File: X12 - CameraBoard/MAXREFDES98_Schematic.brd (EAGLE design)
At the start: 87.8 x 25.4 mm, 26 parts, among them U1 MB110S-TP, U2 MB110S-TP, U3 MAX5969AETB+, U4 MAX17503ATP+

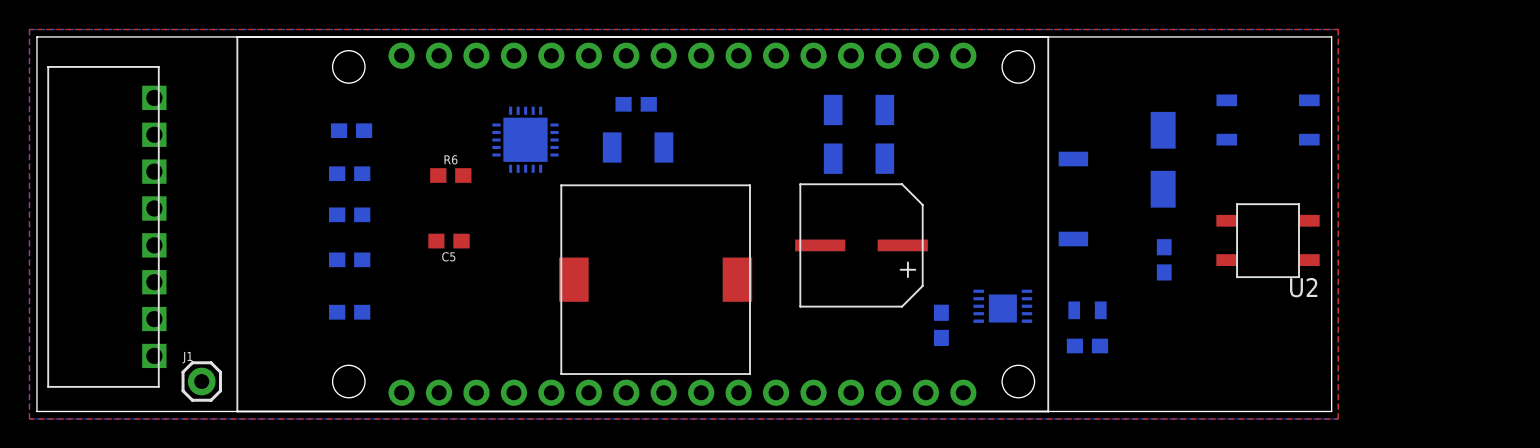
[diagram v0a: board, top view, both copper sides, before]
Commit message: Rerouting
Almost done, just need some clarification on the signals connected to the 8-pin connector before I try routing those. If the signals are as I assumed, the 8-pin connector might need to move to the other side of the board.
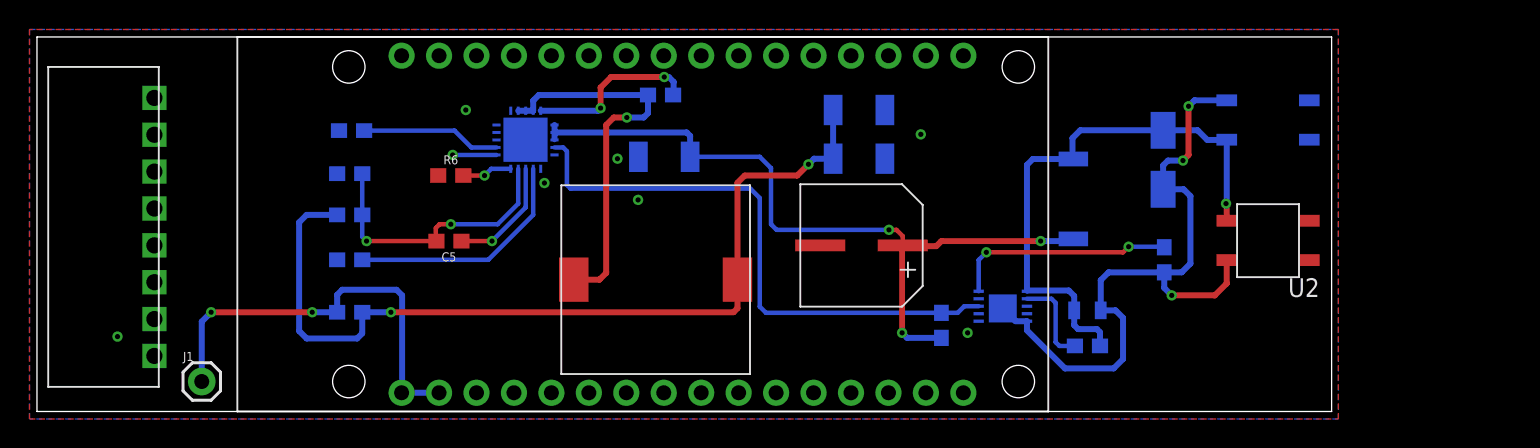
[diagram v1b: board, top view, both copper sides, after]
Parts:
- moved C7 1.89 mm to (42.5, 17.3)
- moved C9 1.77 mm to (42.3, 21.5)
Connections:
- net N$4 renamed CLS
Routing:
- net IND_2_OUT: track 0.00 -> 60.8 mm, vias 0 -> 2
- net VIN: track 0.00 -> 51.8 mm, vias 0 -> 3
- net VSS_EP: track 0.00 -> 47.3 mm, vias 0 -> 3
- net PG_EN/UVLO: track 0.00 -> 39.3 mm
- net VDD: track 0.00 -> 38.0 mm, vias 0 -> 1
- net 5V_OUT: track 0.00 -> 28.6 mm, vias 0 -> 2
- net LX: track 0.00 -> 26.6 mm, vias 0 -> 1
- net FB: track 0.00 -> 19.0 mm, vias 0 -> 2
- net SS: track 0.00 -> 16.0 mm
- net CLS: track 0.00 -> 15.1 mm, vias 0 -> 2
- net BST: track 0.00 -> 11.8 mm, vias 0 -> 2
- net VCC: track 0.00 -> 9.45 mm
- net CF: track 0.00 -> 7.92 mm, vias 0 -> 1
- net DET: track 0.00 -> 6.14 mm
- net RT: track 0.00 -> 3.40 mm, vias 0 -> 1
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
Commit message: Rerouting
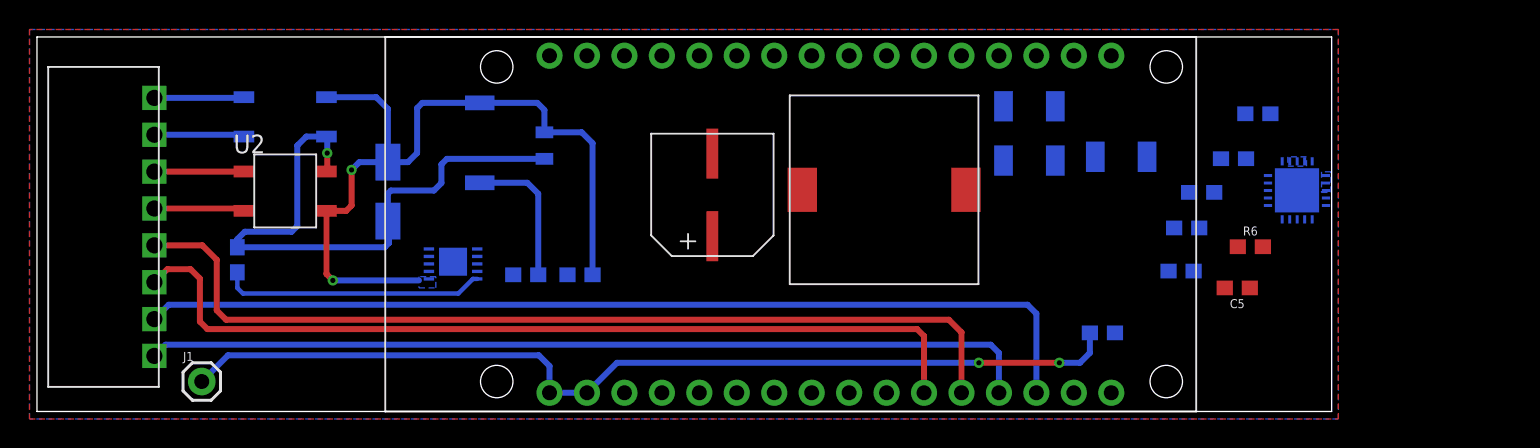
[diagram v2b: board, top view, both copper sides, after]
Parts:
- moved U1 73.8 mm to (13.3, 21.7), turned to 180 degrees
- moved U2 73.7 mm to (13.3, 13.2), turned to 0 degrees
- moved R1 62.9 mm to (13.6, 10.3), turned to 270 degrees
- moved C8 59.8 mm to (81.2, 17.1)
- moved R5 57.8 mm to (79.0, 14.9)
- moved R4 56.8 mm to (78.0, 12.4)
- moved C6 56.4 mm to (77.6, 9.53)
- moved R6 54.4 mm to (82.3, 11.2)
- moved C5 53.6 mm to (81.4, 8.38)
- moved D1 52.6 mm to (27.1, 18.2)
- moved U4 52.4 mm to (87.5, 13.0)
- moved R7 51.1 mm to (72.3, 5.33)
- moved U3 40.8 mm to (26.7, 11.6), turned to 180 degrees
- moved C9 40.5 mm to (82.8, 20.2)
- moved L1 40.4 mm to (32.9, 21.1)
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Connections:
- removed net RXD: CONN.5
- removed net TXD: CONN.6
- new net RD+: CONN.5, U$2.RD+
- new net RD-: CONN.6, U$2.RD-
- new net TD+: CONN.7, U$2.TD+
- new net TD-: CONN.8, U$2.TD-
- net GND: no longer CONN.7, CONN.8
- net RECT1_IN_MINUS: now also CONN.2; no longer CONN.1
- net RECT1_IN_PLUS: now also CONN.1; no longer CONN.2
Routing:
- net TD+: track 0.00 -> 65.8 mm
- net RD+: track 0.00 -> 63.3 mm
- net IND_2_OUT: track 60.8 -> 0.00 mm, vias 2 -> 0
- net TD-: track 0.00 -> 60.5 mm
- net RD-: track 0.00 -> 60.0 mm
- net VIN: track 51.8 -> 9.77 mm, vias 3 -> 0
- net PG_EN/UVLO: track 39.3 -> 0.00 mm
- net 5V_OUT: track 28.6 -> 65.6 mm
- net LX: track 26.6 -> 0.00 mm, vias 1 -> 0
- net FB: track 19.0 -> 0.00 mm, vias 2 -> 0
- net VDD: track 38.0 -> 54.1 mm, vias 1 -> 2
- net SS: track 16.0 -> 0.00 mm
- net BST: track 11.8 -> 0.00 mm, vias 2 -> 0
- net VCC: track 9.45 -> 0.00 mm
- net CF: track 7.92 -> 0.00 mm, vias 1 -> 0
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- added copper zone on layer 16, net LX
- added copper zone on layer 16, net VDD
- added copper zone on layer 16, net VIN

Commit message: Fixing 0-Ohm Resistor stuff
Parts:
- removed J1: (no value), SparkFun-Connectors:1X01
- removed R7: 0, SparkFun-Resistors:0603
- added R10, R11, R8, R9: 0, SparkFun-Resistors:0603
- moved C7 6.49 mm to (67.9, 14.0), turned to 180 degrees
- moved C10 0.74 mm to (67.9, 17.4)
- moved C4 0.65 mm to (67.9, 20.8)
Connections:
- removed net IND_2_OUT: C10.1, C4.1, L2.P$2, R4.2, R7.1
- net 5V_OUT: now also C10.1, C4.1, L2.P$2, R11.1, R4.2, R8.1; no longer J1.1, R7.2
- net GND: now also R10.1, R9.1
- net RECT1_IN_MINUS: now also R10.2
- net RECT1_IN_PLUS: now also R8.2
- net RECT2_IN_MINUS: now also R9.2
- net RECT2_IN_PLUS: now also R11.2
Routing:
- net VIN: track 9.77 -> 50.1 mm, vias 0 -> 2
- net 5V_OUT: track 65.6 -> 104.4 mm, vias 2 -> 3
- net VSS_EP: track 41.2 -> 60.4 mm, vias 1 -> 3
- net PG_EN/UVLO: track 0.00 -> 16.4 mm
- net DET: track 0.00 -> 14.8 mm, vias 0 -> 2
- net RECT2_IN_MINUS: track 6.08 -> 8.61 mm
- net RECT1_IN_PLUS: track 6.09 -> 8.59 mm
- net RECT1_IN_MINUS: track 6.12 -> 8.53 mm
- net RECT2_IN_PLUS: track 6.14 -> 8.48 mm
- added copper zone on layer 16, net DET
- added copper zone on layer 16, net PG_EN/UVLO

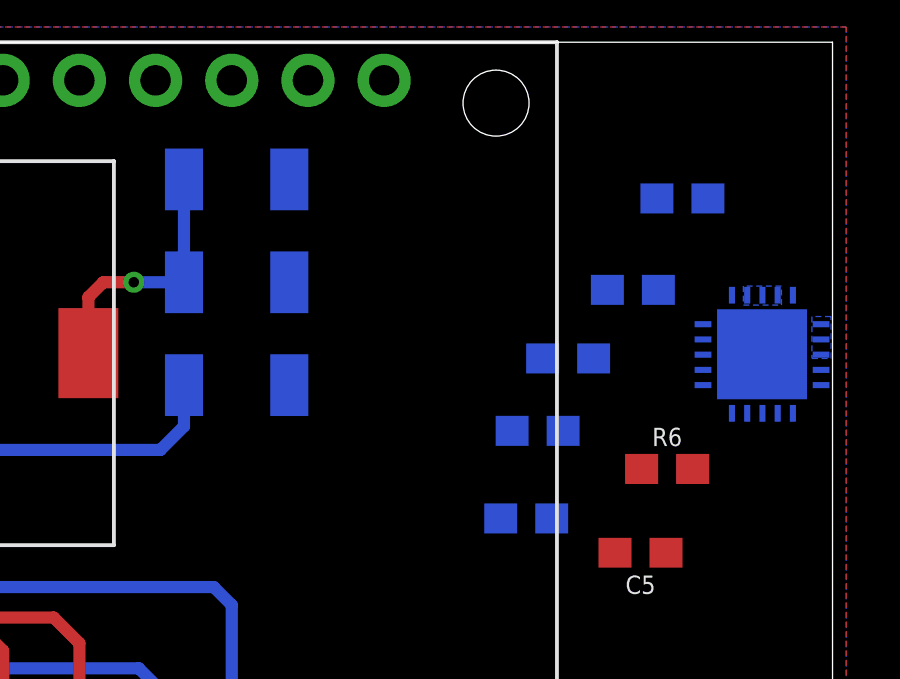
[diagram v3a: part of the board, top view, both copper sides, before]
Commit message: Added New Buck Regultor (needs to be connected with new supporting circuitry)
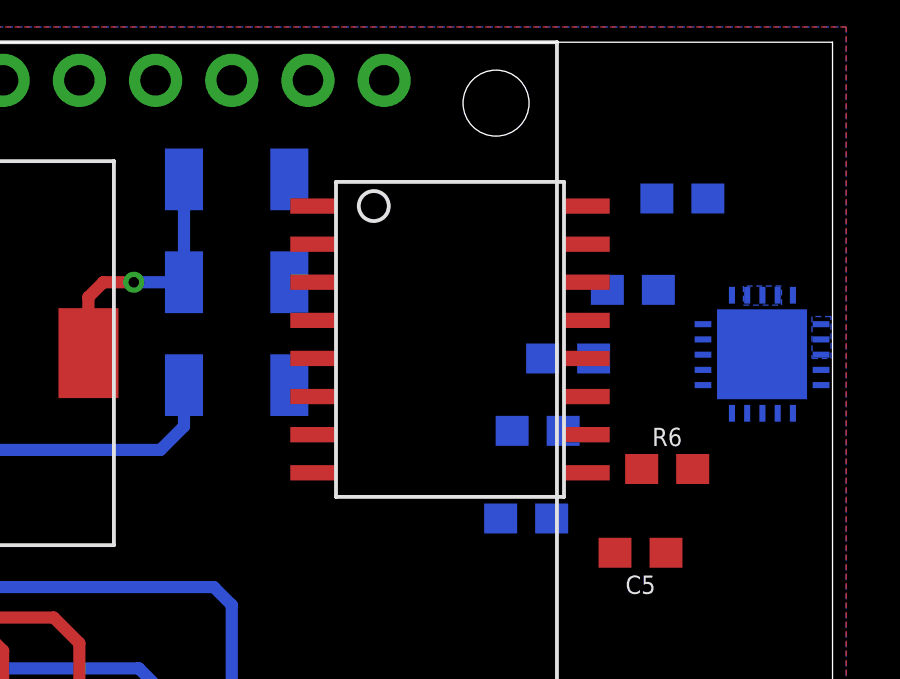
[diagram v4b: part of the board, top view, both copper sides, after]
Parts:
- added U$1: L4978D013TR, Camera_Board_Parts_09_30_2020:L4978D013TR
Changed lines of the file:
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@@
 <attribute name="VALUE" x="4.572" y="14.605" size="0.6096" layer="28" font="vector" ratio="20" rot="MR180" align="top-center"/>
 </element>
+<element name="U$1" library="Camera_Board_Parts_09_30_2020" package="L4978D013TR" value="L4978D013TR" x="75.057" y="15.494" smashed="yes"/>
 </elements>
 <signals>

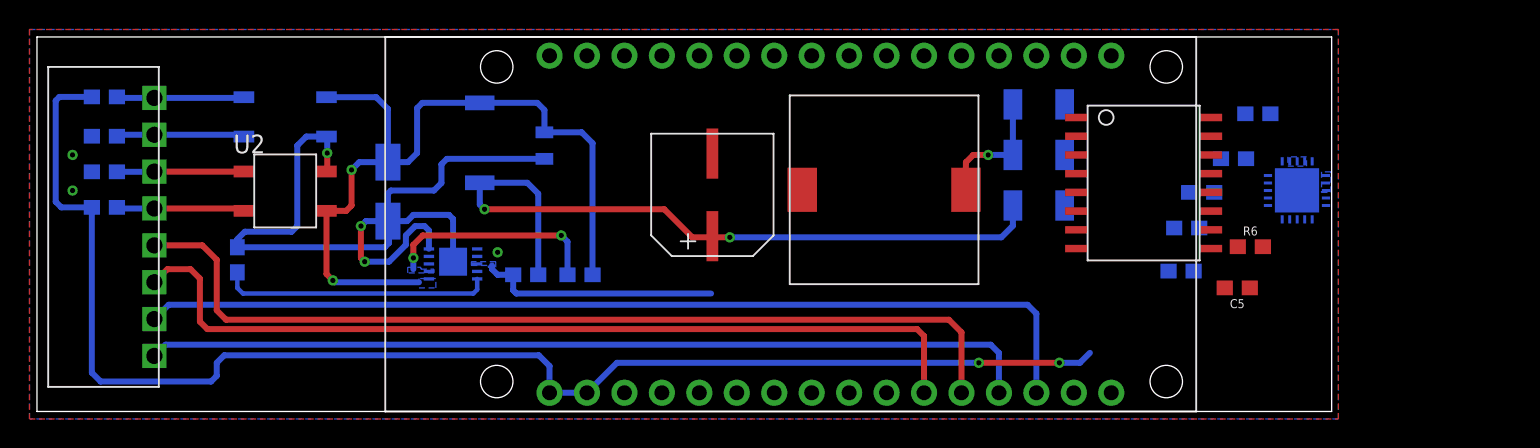
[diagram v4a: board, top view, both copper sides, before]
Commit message: Routing
Definetely need to change buck regulator because of spacing and soldering issues. Will do that soonish.
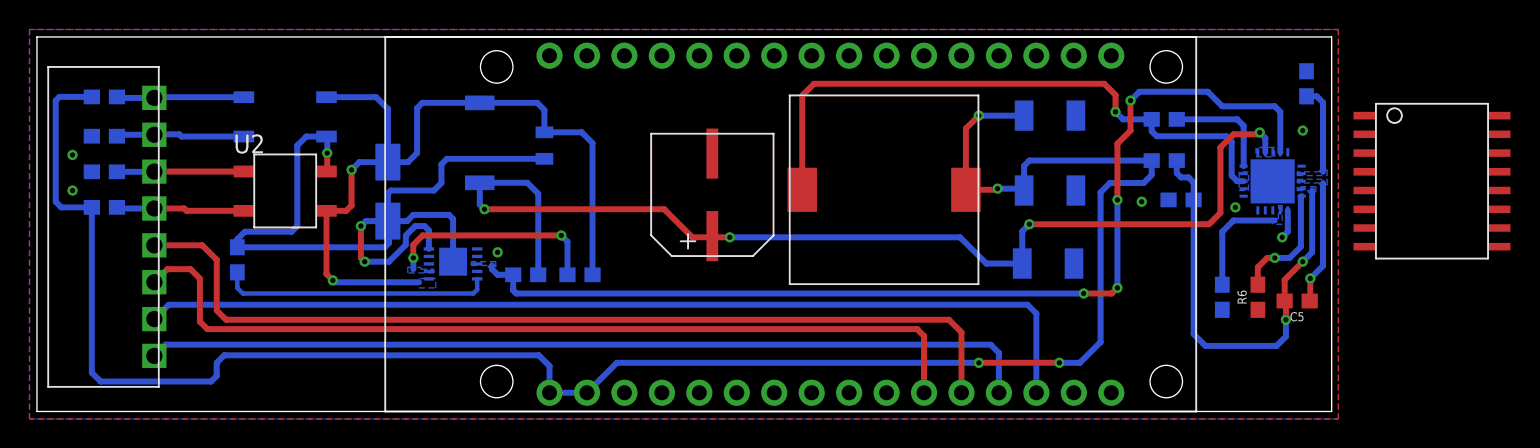
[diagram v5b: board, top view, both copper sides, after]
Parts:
- moved U$1 19.6 mm to (94.6, 15.6)
- moved C6 15.3 mm to (86.1, 22.2), turned to 90 degrees
- moved C8 9.43 mm to (80.4, 7.75), turned to 270 degrees
- moved C9 6.36 mm to (76.5, 19.8)
- moved C4 5.89 mm to (68.7, 15.0)
- moved U4 4.98 mm to (85.9, 17.7), turned to 270 degrees
- moved R4 4.82 mm to (76.5, 17.0)
- moved C5 4.16 mm to (85.5, 7.49)
- moved C7 3.99 mm to (68.6, 10.0)
- moved R6 3.47 mm to (82.8, 7.75), turned to 90 degrees
- moved C10 2.77 mm to (68.7, 20.1)
- moved R5 1.49 mm to (77.6, 14.4)
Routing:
- net PG_EN/UVLO: track 16.4 -> 70.9 mm, vias 0 -> 4
- net LX: track 0.00 -> 41.9 mm, vias 0 -> 1
- net 5V_OUT: track 104.4 -> 134.8 mm, vias 3 -> 4
- net FB: track 0.00 -> 30.1 mm, vias 0 -> 2
- net VIN: track 50.1 -> 75.0 mm, vias 2 -> 4
- net CF: track 0.00 -> 8.37 mm, vias 0 -> 1
- net RT: track 0.00 -> 8.13 mm, vias 0 -> 1
- net VCC: track 0.00 -> 7.47 mm
- net BST: track 0.00 -> 7.46 mm
- net SS: track 0.00 -> 5.99 mm
- net GND: track 0.00 -> 1.99 mm, vias 3 -> 7
- added copper zone on layer 16, net CF
- added copper zone on layer 16, net FB
- added copper zone on layer 16, net SS
- added copper zone on layer 16, net VCC
